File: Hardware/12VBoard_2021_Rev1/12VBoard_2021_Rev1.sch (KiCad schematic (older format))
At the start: 0 parts

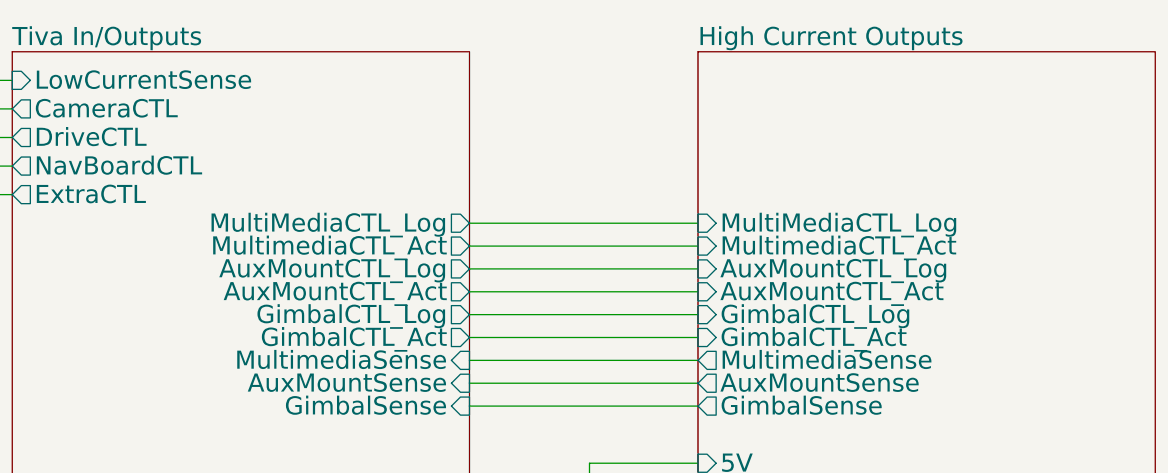
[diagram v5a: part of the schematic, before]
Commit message: admin changes
-current sensing on high current
-fixed traces for current sensing
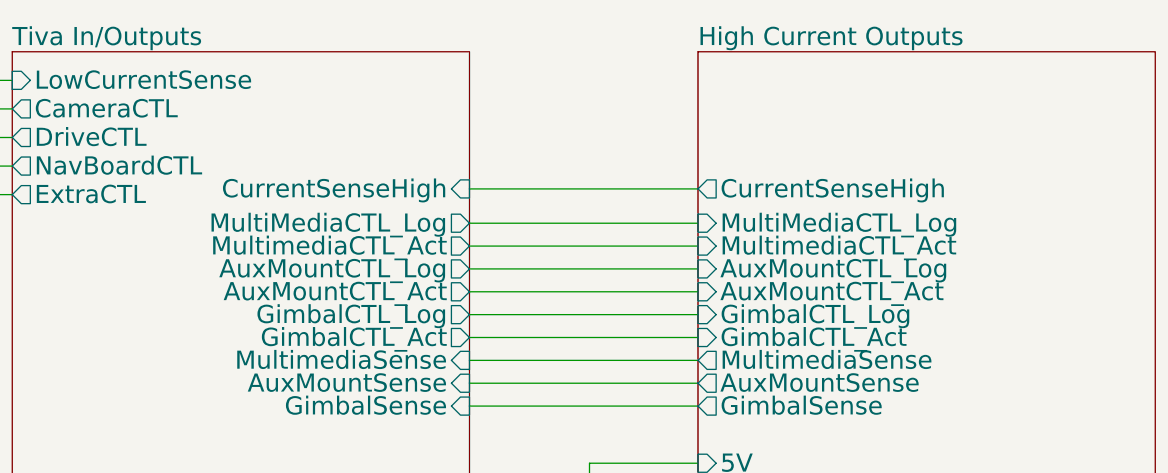
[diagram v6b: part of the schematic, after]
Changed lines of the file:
@@
 EESchema Schematic File Version 4
+LIBS:12VBoard_2021_Rev1-cache
 EELAYER 30 0
 EELAYER END
@@
 F11 "AuxMountSense" O L 8000 3450 79
 F12 "GimbalSense" O L 8000 3550 79
+F13 "CurrentSenseHigh" O L 8000 2600 79
 $EndSheet
 Wire Wire Line
@@
 Wire Wire Line
 	5000 2125 4000 2125
-$Sheet
-S 2000 2000 2000 2000
-U 5F74F223
-F0 "Low Current Outputs" 79
-F1 "Low Current Outputs.sch" 79
-F2 "PackVoltage" I R 4000 3900 79
-F3 "5V" O R 4000 3800 79
-F4 "CameraCTL" I R 4000 2250 79
-F5 "NavCTL" I R 4000 2500 79
-F6 "CurrentSense" O R 4000 2125 79
-F7 "ExtraCTL" I R 4000 2625 79
-F8 "DriveCTL" I R 4000 2375 79
-$EndSheet
 $Sheet
 S 5000 2000 2000 2000
@@
 F14 "AuxMountSense" I R 7000 3450 79
 F15 "GimbalSense" I R 7000 3550 79
+F16 "CurrentSenseHigh" I R 7000 2600 79
 $EndSheet
 Wire Wire Line
@@
 Wire Wire Line
 	7000 3550 8000 3550
+$Sheet
+S 2000 2000 2000 2000
+U 5F74F223
+F0 "Low Current Outputs" 79
+F1 "Low Current Outputs.sch" 79
+F2 "PackVoltage" I R 4000 3900 79
+F3 "5V" O R 4000 3800 79
+F4 "CameraCTL" I R 4000 2250 79
+F5 "NavCTL" I R 4000 2500 79
+F6 "CurrentSense" O R 4000 2125 79
+F7 "ExtraCTL" I R 4000 2625 79
+F8 "DriveCTL" I R 4000 2375 79
+$EndSheet
+Wire Wire Line
+	8000 2600 7000 2600
 $EndSCHEMATC

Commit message: Fixed problem
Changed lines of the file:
@@
 Wire Wire Line
 	4525 4525 4525 3800
-$Sheet
-S 8000 2000 2000 2000
-U 5F74F36B
-F0 "High Current Outputs" 79
-F1 "High Current Outputs.sch" 79
-F2 "PackVoltage" I L 8000 3900 79
-F3 "5V" I L 8000 3800 79
-F4 "MultiMediaCTL_Log" I L 8000 2750 79
-F5 "MultimediaCTL_Act" I L 8000 2850 79
-F6 "AuxMountCTL_Log" I L 8000 2950 79
-F7 "AuxMountCTL_Act" I L 8000 3050 79
-F8 "GimbalCTL_Log" I L 8000 3150 79
-F9 "GimbalCTL_Act" I L 8000 3250 79
-F10 "MultimediaSense" O L 8000 3350 79
-F11 "AuxMountSense" O L 8000 3450 79
-F12 "GimbalSense" O L 8000 3550 79
-F13 "CurrentSenseHigh" O L 8000 2600 79
-$EndSheet
 Wire Wire Line
 	5000 2250 4000 2250
@@
 F14 "AuxMountSense" I R 7000 3450 79
 F15 "GimbalSense" I R 7000 3550 79
-F16 "CurrentSenseHigh" I R 7000 2600 79
+F16 "BuckCTL" O R 7000 2675 50
 $EndSheet
 Wire Wire Line
@@
 F7 "ExtraCTL" I R 4000 2625 79
 F8 "DriveCTL" I R 4000 2375 79
+F9 "12VLogic" O R 4000 3700 50
+F10 "12VActuation" I R 4000 3635 50
 $EndSheet
 Wire Wire Line
-	8000 2600 7000 2600
+	8000 3655 7060 3655
+Wire Wire Line
+	7060 3655 7060 4170
+Wire Wire Line
+	7060 4170 4910 4170
+Wire Wire Line
+	4910 4170 4910 3635
+Wire Wire Line
+	4910 3635 4000 3635
+Wire Wire Line
+	4000 3700 4725 3700
+Wire Wire Line
+	4725 3700 4725 4340
+Wire Wire Line
+	4725 4340 7250 4340
+Wire Wire Line
+	7250 4340 7250 3720
+Wire Wire Line
+	7250 3720 8000 3720
+$Sheet
+S 8000 2000 2000 2000
+U 5F74F36B
+F0 "High Current Outputs" 79
+F1 "High Current Outputs.sch" 79
+F2 "PackVoltage" I L 8000 3900 79
+F3 "5V" I L 8000 3800 79
+F4 "MultiMediaCTL_Log" I L 8000 2750 79
+F5 "MultimediaCTL_Act" I L 8000 2850 79
+F6 "AuxMountCTL_Log" I L 8000 2950 79
+F7 "AuxMountCTL_Act" I L 8000 3050 79
+F8 "GimbalCTL_Log" I L 8000 3150 79
+F9 "GimbalCTL_Act" I L 8000 3250 79
+F10 "MultimediaSense" O L 8000 3350 79
+F11 "AuxMountSense" O L 8000 3450 79
+F12 "GimbalSense" O L 8000 3550 79
+F13 "12VLogic" I L 8000 3720 50
+F14 "12VActuation" O L 8000 3655 50
+F15 "BuckCTL" I L 8000 2675 50
+$EndSheet
+Wire Wire Line
+	7000 2675 8000 2675
 $EndSCHEMATC
